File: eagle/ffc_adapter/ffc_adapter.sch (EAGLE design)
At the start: 10 parts, among them J1 FH12-6S-0.5SH(55), J2 FH12-6S-0.5SH(55), J3 FH12-6S-0.5SH(55), J4 FH12-6S-0.5SH(55), J5 FH12-6S-0.5SH(55)

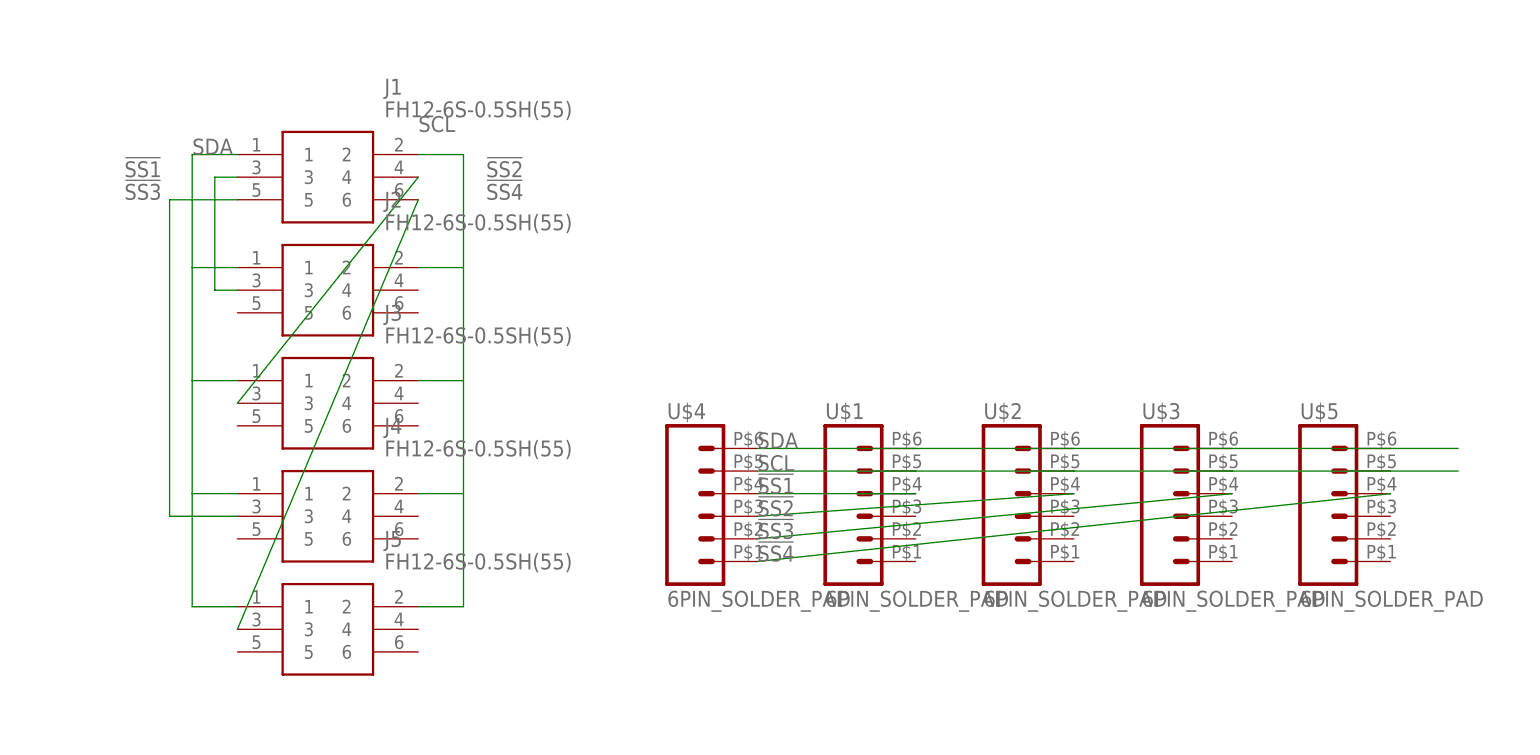
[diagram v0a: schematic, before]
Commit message: Update the FFC adapter to use bottom contact connectors;
The previous design had the pin orders to match those in the connector
board. When using a forward direction cable (contacts on the same side
on both ends) and a top contact connector on both ends, the pin order
would get mirrored. Because the forward direction cable and the top
contact connectors are (supposedly?) the norm, it's probably better to
just reverse the pins on the adapter in order to be able to use the same
connectors and cables everywhere.
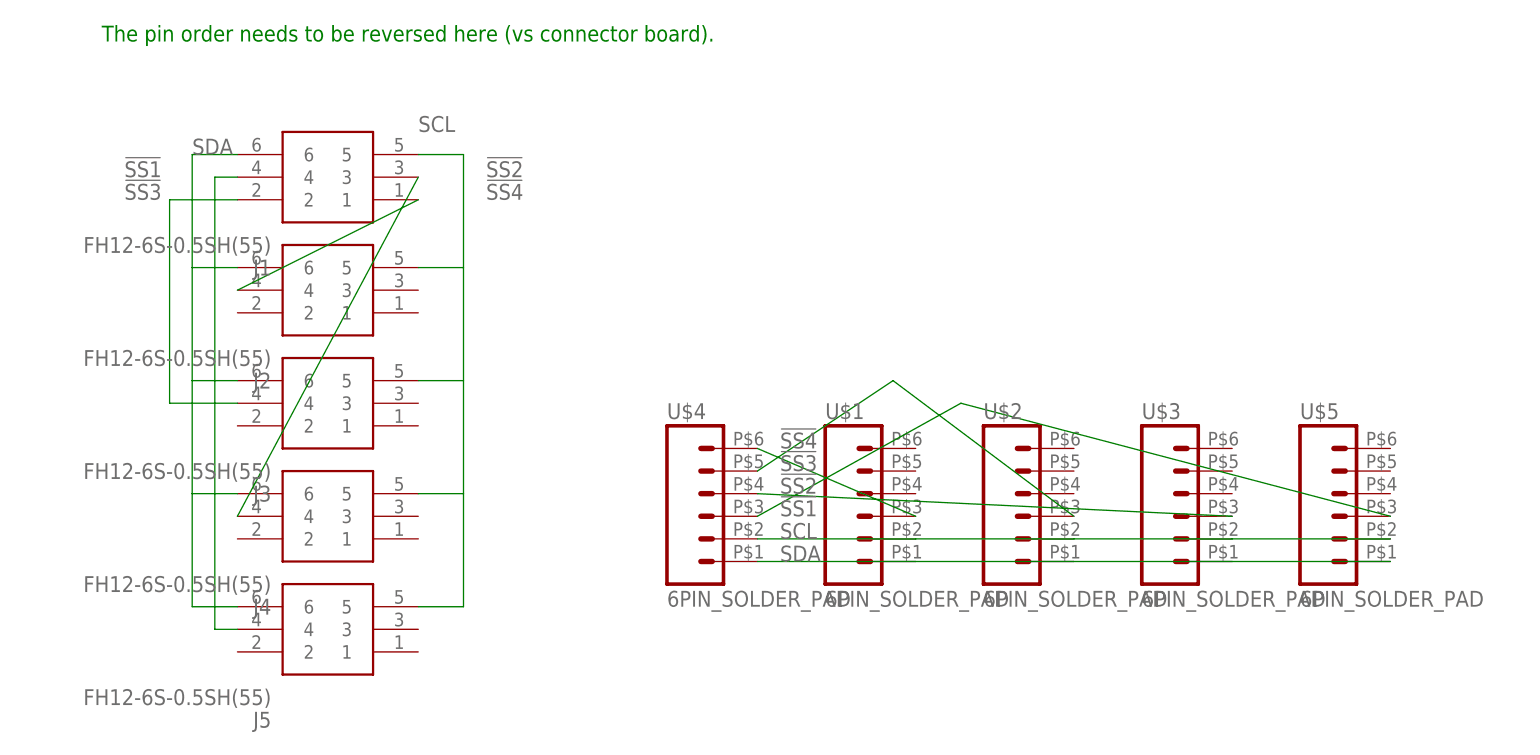
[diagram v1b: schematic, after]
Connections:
- net !SS1: now also J1.4, J5.4, U$4.3, U$5.3; no longer J1.3, J2.3, U$1.4, U$4.4
- net !SS2: now also J1.3, J4.4, U$3.3, U$4.4; no longer J1.4, J3.3, U$2.4, U$4.3
- net !SS3: now also J1.2, J3.4, U$2.3, U$4.5; no longer J1.5, J4.3, U$3.4, U$4.2
- net !SS4: now also J1.1, J2.4, U$1.3, U$4.6; no longer J1.6, J5.3, U$4.1, U$5.4
- net SCL: now also J1.5, J2.5, J3.5, J4.5, J5.5, U$1.2, U$2.2, U$3.2, U$4.2, U$5.2; no longer J1.2, J2.2, J3.2, J4.2, J5.2, U$1.5, U$2.5, U$3.5, U$4.5, U$5.5
- net SDA: now also J1.6, J2.6, J3.6, J4.6, J5.6, U$1.1, U$2.1, U$3.1, U$4.1, U$5.1; no longer J1.1, J2.1, J3.1, J4.1, J5.1, U$1.6, U$2.6, U$3.6, U$4.6, U$5.6
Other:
- note added: "The pin order needs to be reversed here (vs connector board)."
- moved on the sheet: J1, J2, J3, J4, J5
